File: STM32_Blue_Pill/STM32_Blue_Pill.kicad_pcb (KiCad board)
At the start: 2 copper layers, 19.3 x 52.1 mm, 31 parts, among them J1 BootJumper, J2 Conn_01x20, J3 Conn_01x20, J4 Conn_02x05_Odd_Even, J7 USB_B_Micro, SW1 SW_Push, U1 MCP1700-3302E_SOT23, U4 STM32F103C8Tx, Y1 8M, Y2 32.768K

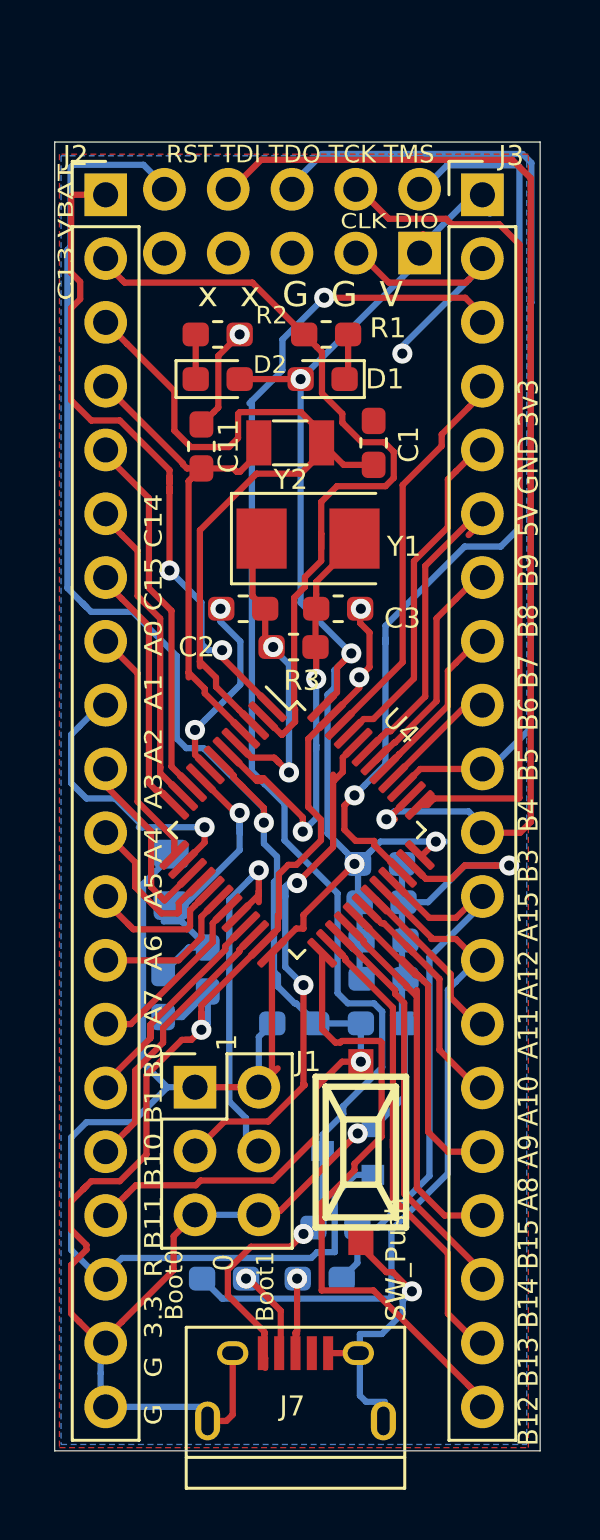
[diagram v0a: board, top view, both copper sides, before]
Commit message: STM32_Blue_Pill: Move all vias out of pads for SMT
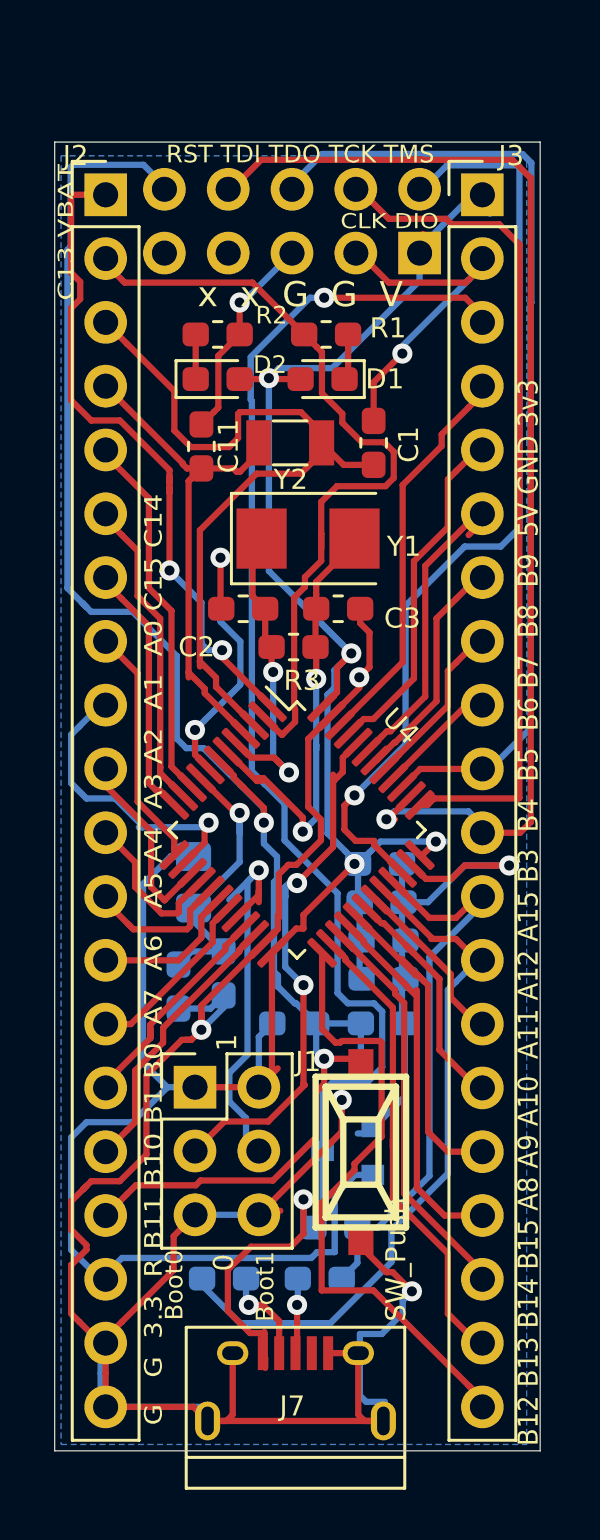
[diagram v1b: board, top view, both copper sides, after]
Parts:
- moved R7 0.90 mm to (32.2, 57.4)
- moved C8 0.70 mm to (31.6, 61.5)
- moved C9 0.65 mm to (33.4, 61.0)
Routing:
- net GND: track 122.5 -> 151.1 mm, vias 10 -> 9
- net VCC: track 101.3 -> 107.5 mm
- net 5V: track 57.9 -> 61.8 mm
- net NRST: track 64.9 -> 67.2 mm
- net Net-(C8-Pad1): track 13.6 -> 11.7 mm
- net BOOT1: track 15.4 -> 17.1 mm
- removed copper zone on F.Cu, net GND
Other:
- board text added: "LQFP48 STM32 board v0.3"
- board text removed: "LQFP48 STM32/GD32 board v0.2"

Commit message: STM32_Blue_Pill: Move all resisters and capacitors to same side for JLC SMT
Signed-off-by: Zamir SUN <sztsian@gmail.com>
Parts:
- C1, C11, C2, C3, R1, R2, R3: moved to B.Cu
- moved C3 5.80 mm to (41.0, 51.4), turned to 270 degrees
- moved C2 5.35 mm to (34.6, 51.8)
- moved R3 4.65 mm to (40.8, 47.9), turned to 270 degrees
- moved C1 1.79 mm to (41.0, 39.2)
- moved R2 1.31 mm to (32.8, 36.8)
- moved R1 1.26 mm to (38.2, 36.6)
- moved C11 0.45 mm to (32.1, 39.9), turned to 270 degrees
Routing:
- net GND: track 151.1 -> 176.1 mm, vias 9 -> 7
- net VCC: track 107.5 -> 132.2 mm
- net Net-(C2-Pad1): track 12.8 -> 20.8 mm
- net Net-(C3-Pad1): track 17.7 -> 22.8 mm, vias 2 -> 3
- net PC15: track 20.9 -> 24.8 mm
- net PA13-SWDIO-TMS: track 37.5 -> 39.5 mm
- net NRST: track 67.2 -> 69.1 mm
- net Net-(D1-Pad1): track 1.84 -> 3.40 mm, vias 0 -> 1
- net Net-(D2-Pad1): track 1.78 -> 3.31 mm, vias 0 -> 1
- net 5V: track 61.8 -> 63.0 mm
- net PC14: track 31.3 -> 30.3 mm, vias 0 -> 1
- net PC13: track 32.0 -> 32.3 mm, vias 0 -> 1
